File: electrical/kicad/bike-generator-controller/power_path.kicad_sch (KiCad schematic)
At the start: 8 parts, among them J1 DC_GEN_IN / DIRECT DC VARIANT, J2 PHOENIX 1711725 / BUCK_IN, J8 3PH_GEN_IN (1=U 2=V 3=W)

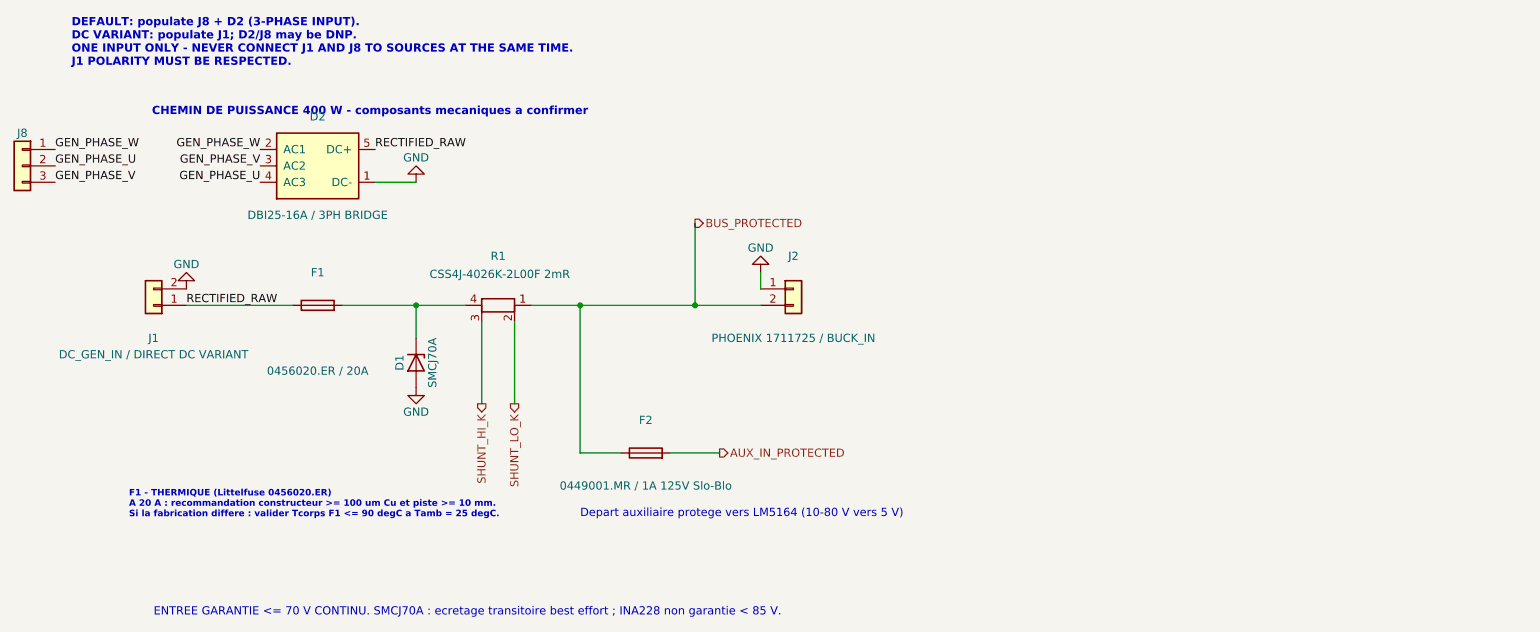
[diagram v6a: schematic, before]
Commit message: feat(controller): finalize V1 design and sourcing
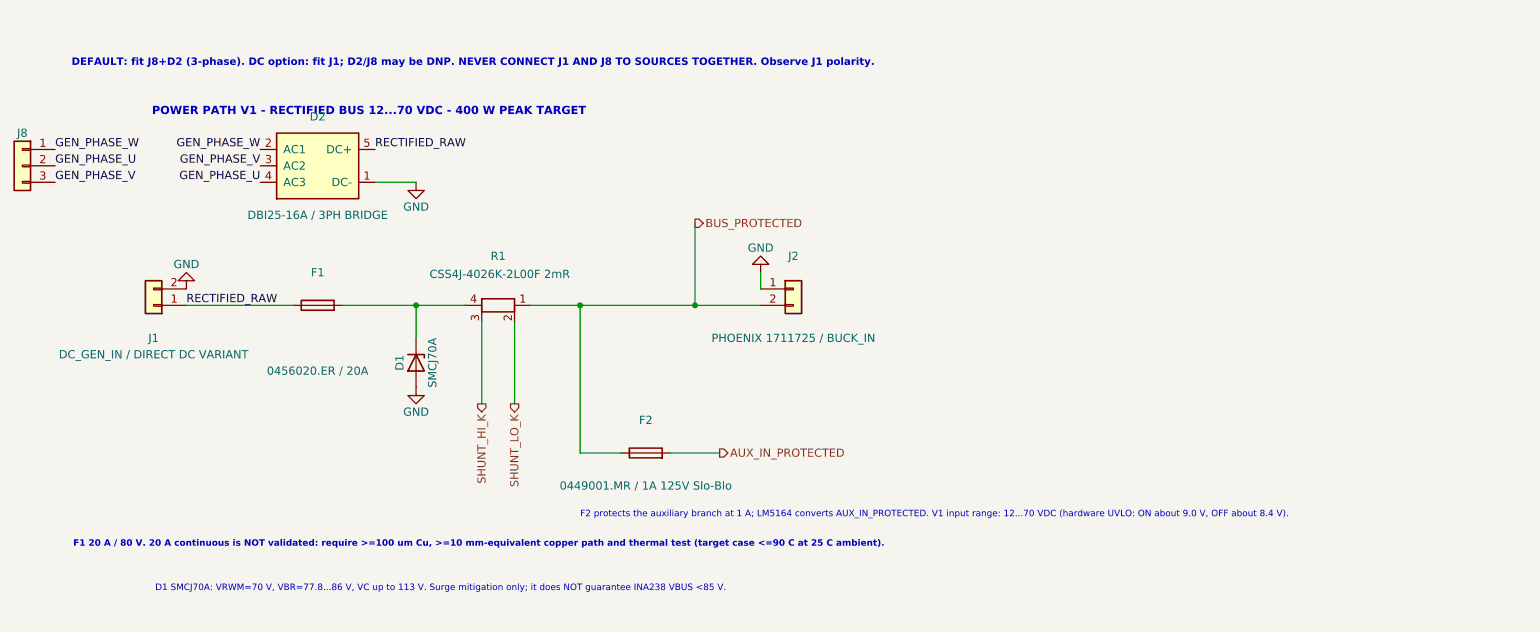
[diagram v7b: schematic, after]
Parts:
- J8: value 3PH_GEN_IN (1=U 2=V 3=W) -> 3PH_GEN_IN (1=W 2=U 3=V)
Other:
- note added: "D1 SMCJ70A: VRWM=70 V, VBR=77.8...86 V, VC up to 113 V. Surge mitigation only; it does NOT guarantee INA238 VBUS <85 V."
- note added: "DEFAULT: fit J8+D2 (3-phase). DC option: fit J1; D2/J8 may be DNP. NEVER CONNECT J1 AND J8 TO SOURCES TOGETHER. Observe J1 polarity."
- note added: "F1 20 A / 80 V. 20 A continuous is NOT validated: require >=100 um Cu, >=10 mm-equivalent copper path and thermal test (target case <=90 C at 25 C ambient)."
- note added: "F2 protects the auxiliary branch at 1 A; LM5164 converts AUX_IN_PROTECTED. V1 input range: 12...70 VDC (hardware UVLO: ON about 9.0 V, OFF about 8.4 V)."
- note added: "POWER PATH V1 - RECTIFIED BUS 12...70 VDC - 400 W PEAK TARGET"
- note removed: "CHEMIN DE PUISSANCE 400 W - composants mecaniques a confirmer"
- note removed: "DEFAULT: populate J8 + D2 (3-PHASE INPUT). DC VARIANT: populate J1; D2/J8 may be DNP. ONE INPUT ONLY - NEVER CONNECT J1 AND J8 TO SOURCES AT THE SAME TIME. J1 POLARITY MUST BE RESPECTED."
- note removed: "Depart auxiliaire protege vers LM5164 (10-80 V vers 5 V)"
- note removed: "ENTREE GARANTIE <= 70 V CONTINU. SMCJ70A : ecretage transitoire best effort ; INA228 non garantie < 85 V."
- note removed: "F1 - THERMIQUE (Littelfuse 0456020.ER) A 20 A : recommandation constructeur >= 100 um Cu et piste >= 10 mm. Si la fabrication differe : valider Tcorps F1 <= 90 degC a Tamb = 25 degC."
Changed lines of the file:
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@@
 	(generator_version "10.0")
 	(paper "A4")
-	(text "F1 - THERMIQUE (Littelfuse 0456020.ER)\nA 20 A : recommandation constructeur >= 100 um Cu et piste >= 10 mm.\nSi la fabrication differe : valider Tcorps F1 <= 90 degC a Tamb = 25 degC."
+	(text "F2 protects the auxiliary branch at 1 A; LM5164 converts AUX_IN_PROTECTED. V1 input range: 12...70 VDC (hardware UVLO: ON about 9.0 V, OFF about 8.4 V)."
 		(exclude_from_sim no)
-		(at 52.07 109.22 0)
+		(at 121.92 109.22 0)
 		(effects
 			(font
 				(size 1 1)
-				(bold yes)
 			)
 			(justify left bottom)
 		)
 	)
-	(text "DEFAULT: populate J8 + D2 (3-PHASE INPUT).\nDC VARIANT: populate J1; D2/J8 may be DNP.\nONE INPUT ONLY - NEVER CONNECT J1 AND J8 TO SOURCES AT THE SAME TIME.\nJ1 POLARITY MUST BE RESPECTED."
-		(exclude_from_sim no)
-		(at 43.18 39.37 0)
-		(effects
-			(font
-				(size 1.27 1.27)
-				(bold yes)
-			)
-			(justify left bottom)
-		)
-	)
-	(text "ENTREE GARANTIE <= 70 V CONTINU. SMCJ70A : ecretage transitoire best effort ; INA228 non garantie < 85 V."
-		(exclude_from_sim no)
-		(at 55.88 124.46 0)
-		(effects
-			(font
-				(size 1.27 1.27)
-			)
-			(justify left bottom)
-		)
-	)
-	(text "CHEMIN DE PUISSANCE 400 W - composants mecaniques a confirmer"
+	(text "POWER PATH V1 - RECTIFIED BUS 12...70 VDC - 400 W PEAK TARGET"
 		(exclude_from_sim no)
 		(at 55.626 46.99 0)
@@
 		)
 	)
-	(text "Depart auxiliaire protege vers LM5164 (10-80 V vers 5 V)"
+	(text "F1 20 A / 80 V. 20 A continuous is NOT validated: require >=100 um Cu, >=10 mm-equivalent copper path and thermal test (target case <=90 C at 25 C ambient)."
 		(exclude_from_sim no)
-		(at 121.92 109.22 0)
+		(at 43.434 113.792 0)
 		(effects
 			(font
-				(size 1.27 1.27)
+				(size 1 1)
+				(bold yes)
+			)
+			(justify left bottom)
+		)
+	)
+	(text "DEFAULT: fit J8+D2 (3-phase). DC option: fit J1; D2/J8 may be DNP. NEVER CONNECT J1 AND J8 TO SOURCES TOGETHER. Observe J1 polarity."
+		(exclude_from_sim no)
+		(at 43.18 39.37 0)
+		(effects
+			(font
+				(size 1.15 1.15)
+				(bold yes)
 			)
 			(justify left bottom)
@@
 		)
 	)
+  (text "D1 SMCJ70A: VRWM=70 V, VBR=77.8...86 V, VC up to 113 V. Surge mitigation only; it does NOT guarantee INA238 VBUS <85 V."
+    (at 56.134 120.65 0)
+    (effects (font (size 1 1)) (justify left bottom))
+  )
 	(symbol
 		(lib_id "Device:R_Shunt")
@@
 			)
 		)
-		(property "Value" "3PH_GEN_IN (1=U 2=V 3=W)"
+		(property "Value" "3PH_GEN_IN (1=W 2=U 3=V)"
 			(at 14.224 64.008 0)
 			(hide yes)
@@
 	(symbol
 		(lib_id "power:GND")
-		(at 96.52 57.15 180)
+		(at 96.52 57.15 0)
 		(unit 1)
 		(body_style 1)
@@
 		(dnp no)
 		(property "Reference" "#PWR004"
-			(at 96.52 50.8 0)
+			(at 96.52 63.5 0)
 			(hide yes)
 			(show_name no)
@@
 		)
 		(property "Value" "GND"
-			(at 96.52 53.34 0)
-			(show_name no)
-			(do_not_autoplace no)
+			(at 96.52 60.96 0)
+			(show_name no)
+			(do_not_autoplace no)
